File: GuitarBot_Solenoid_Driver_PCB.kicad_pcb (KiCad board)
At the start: 2 copper layers, 46 parts, among them J1 Screw_Terminal_01x02, J2 Screw_Terminal_01x16, J3 Screw_Terminal_01x16, J4 Screw_Terminal_01x04, Q1 NMOS, Q10 NMOS, Q11 NMOS, Q12 NMOS, Q13 NMOS, Q14 NMOS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

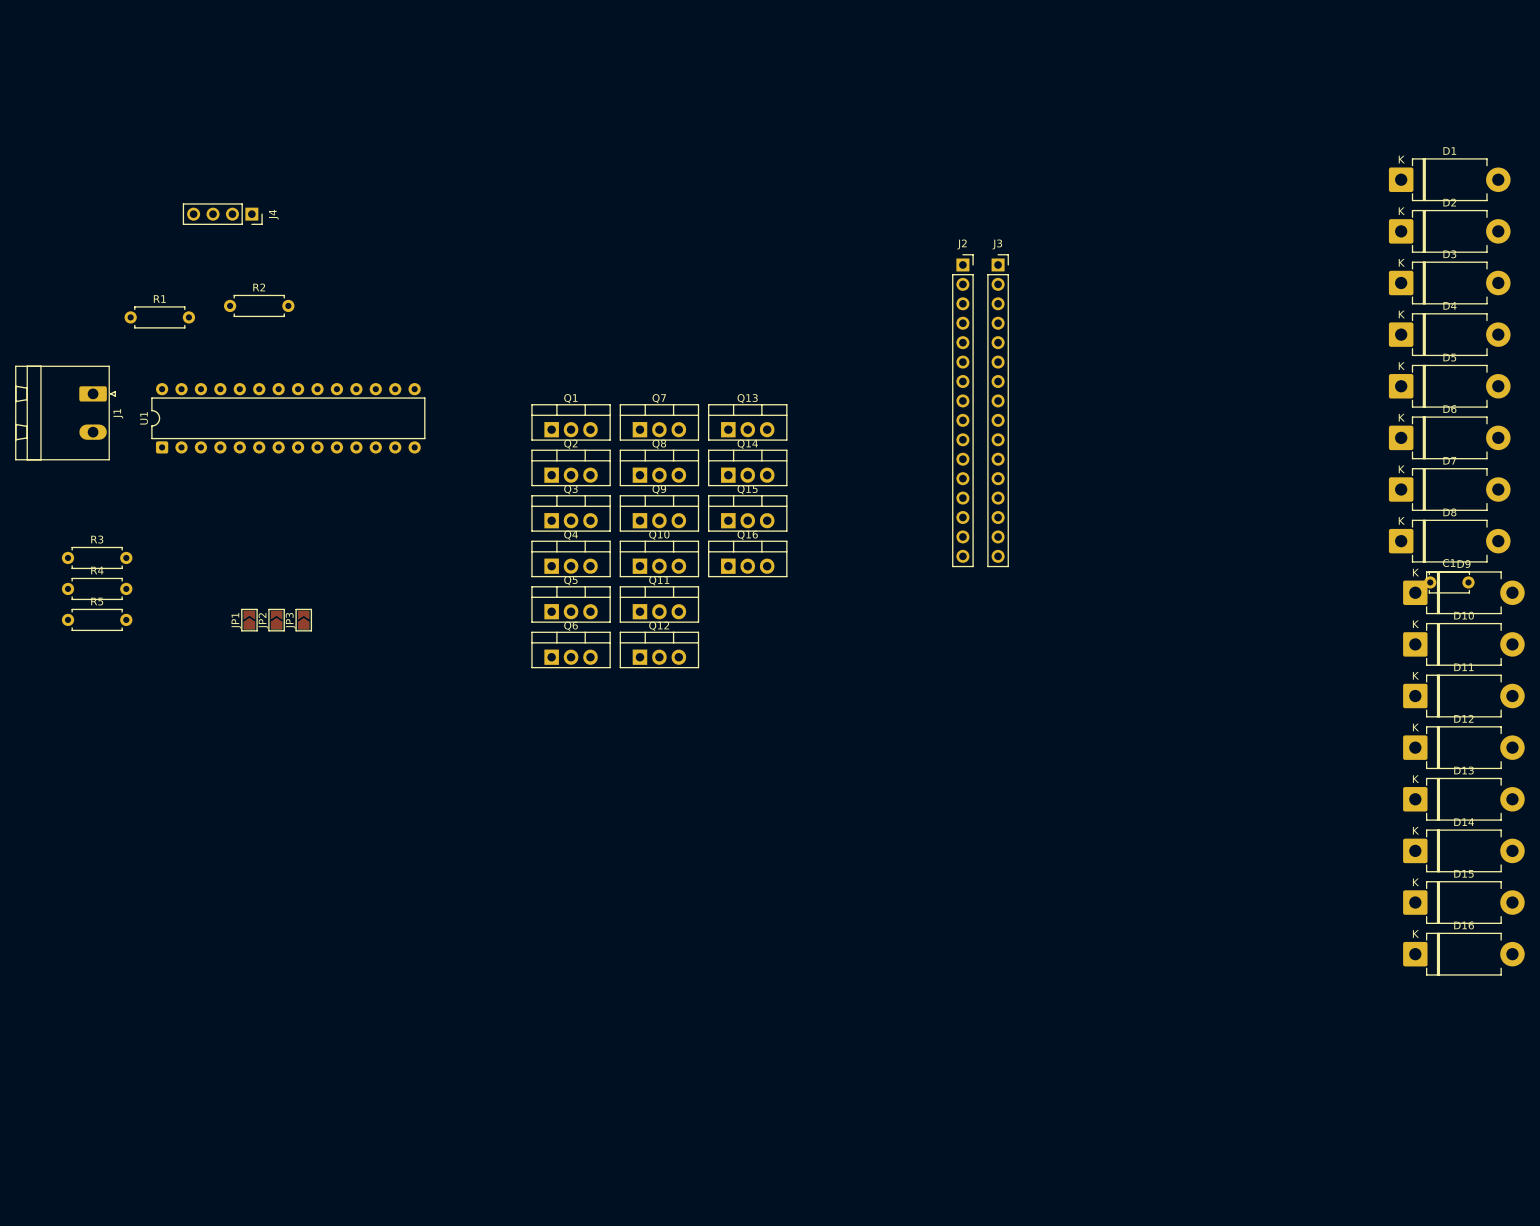
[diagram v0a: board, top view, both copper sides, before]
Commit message: Started pcb layout and updated schematic
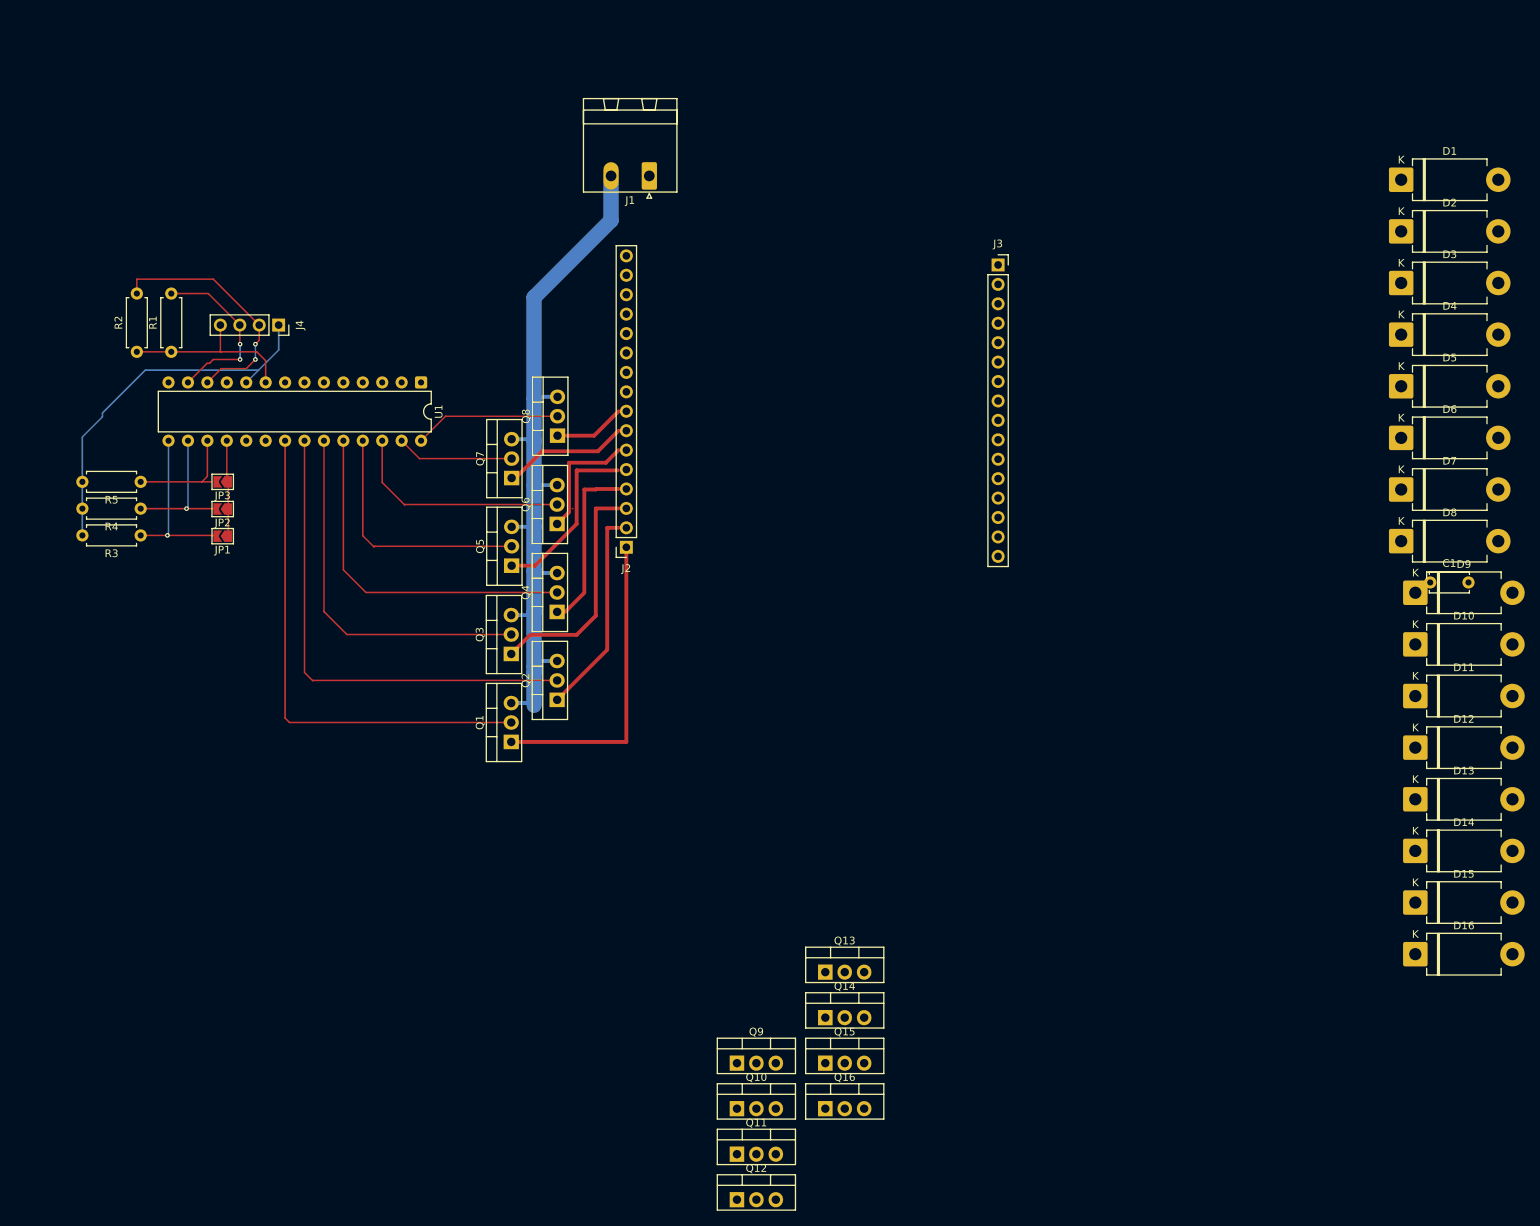
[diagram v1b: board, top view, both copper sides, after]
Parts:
- moved J1 78.1 mm to (122.0, 55.5), turned to 180 degrees
- moved Q14 72.0 mm to (145.0, 165.6)
- moved Q11 72.0 mm to (133.5, 183.4)
- moved Q12 72.0 mm to (133.5, 189.3)
- moved Q13 72.0 mm to (145.0, 159.6)
- moved Q15 72.0 mm to (145.0, 171.5)
- moved Q9 72.0 mm to (133.5, 171.5)
- moved Q10 72.0 mm to (133.5, 177.4)
- moved Q16 72.0 mm to (145.0, 177.4)
- moved J2 57.4 mm to (119.0, 104.0), turned to 180 degrees
- moved Q1 41.2 mm to (104.0, 129.5), turned to 90 degrees
- moved U1 34.9 mm to (92.2, 82.5), turned to -90 degrees
- moved Q2 29.4 mm to (110.0, 124.0), turned to 90 degrees
- moved JP3 21.0 mm to (66.2, 95.5), turned to 180 degrees
- moved R5 20.4 mm to (55.5, 95.5), turned to 180 degrees
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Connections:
- Q1 pad 1: Net-(D8-A) -> Net-(D1-A)
- Q2 pad 1: Net-(D7-A) -> Net-(D2-A)
- Q3 pad 1: Net-(D6-A) -> Net-(D3-A)
- Q4 pad 1: Net-(D5-A) -> Net-(D4-A)
- Q5 pad 1: Net-(D4-A) -> Net-(D5-A)
- Q6 pad 1: Net-(D3-A) -> Net-(D6-A)
- Q7 pad 1: Net-(D2-A) -> Net-(D7-A)
- Q8 pad 1: Net-(D1-A) -> Net-(D8-A)
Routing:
- net GNDPWR: track 0.00 -> 153.1 mm
- net /Sol1: track 0.00 -> 66.1 mm
- net /Sol2: track 0.00 -> 63.8 mm
- net /Sol3: track 0.00 -> 48.1 mm
- net /Sol4: track 0.00 -> 46.1 mm
- net Net-(D1-A): track 0.00 -> 40.5 mm
- net +3.3V: track 0.00 -> 37.0 mm
- net /SDK: track 0.00 -> 32.6 mm, vias 0 -> 2
- net /Sol5: track 0.00 -> 32.5 mm
- net Net-(D3-A): track 0.00 -> 30.2 mm
- net /Sol6: track 0.00 -> 29.6 mm
- net Net-(D2-A): track 0.00 -> 26.7 mm
- net Net-(D5-A): track 0.00 -> 23.3 mm
- net /SDA: track 0.00 -> 23.2 mm, vias 0 -> 2
- net Net-(D4-A): track 0.00 -> 22.6 mm
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
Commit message: Fixed NMOS symbol in schematic. Finished wiring the PCB
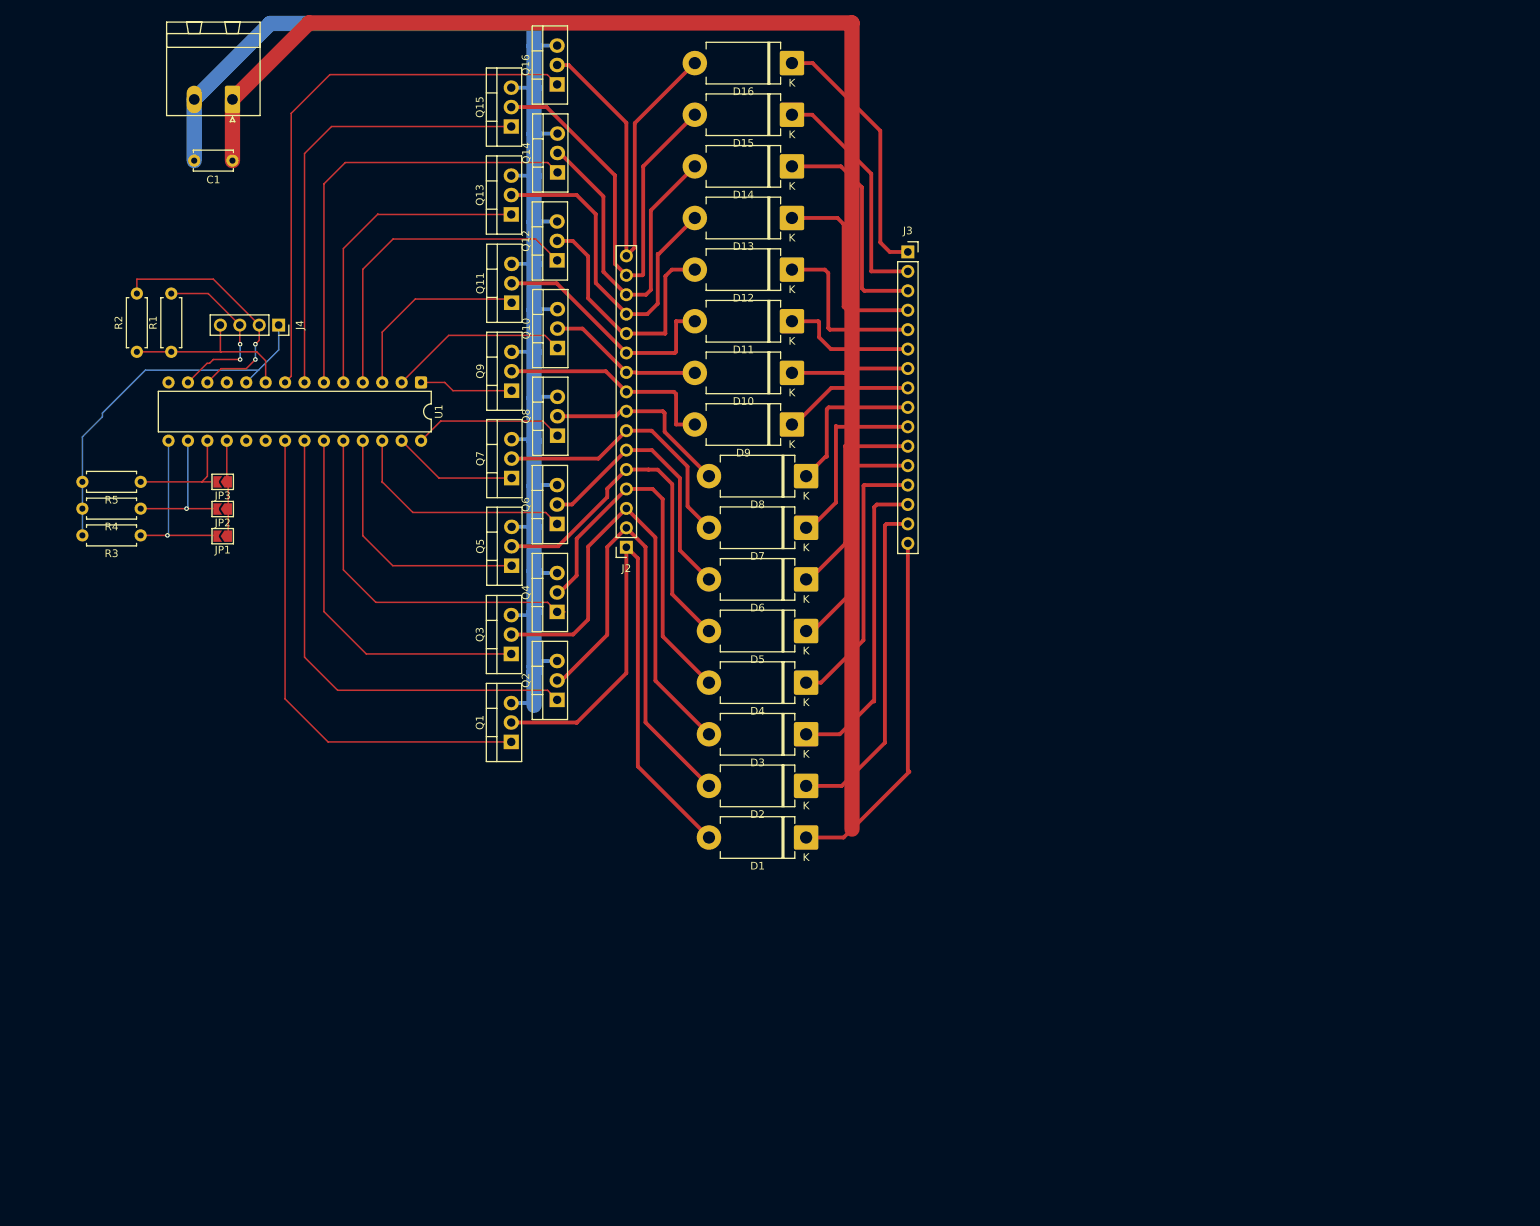
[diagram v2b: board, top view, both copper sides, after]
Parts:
- moved C1 166.0 mm to (67.5, 53.5), turned to 180 degrees
- moved D16 142.2 mm to (140.7, 40.8), turned to 180 degrees
- moved Q16 138.4 mm to (110.0, 43.5), turned to 90 degrees
- moved D15 131.3 mm to (140.7, 47.5), turned to 180 degrees
- moved Q15 129.2 mm to (104.0, 49.0), turned to 90 degrees
- moved Q12 125.0 mm to (110.0, 66.5), turned to 90 degrees
- moved D14 121.0 mm to (140.7, 54.2), turned to 180 degrees
- moved D1 116.0 mm to (142.5, 142.0), turned to 180 degrees
- moved Q14 115.9 mm to (110.0, 55.0), turned to 90 degrees
- moved Q11 115.2 mm to (104.0, 72.1), turned to 90 degrees
- moved D13 111.4 mm to (140.7, 61.0), turned to 180 degrees
- moved Q13 107.2 mm to (104.0, 60.5), turned to 90 degrees
- moved D2 106.3 mm to (142.5, 135.2), turned to 180 degrees
- moved D12 102.7 mm to (140.7, 67.8), turned to 180 degrees
- moved Q10 102.2 mm to (110.0, 78.0), turned to 90 degrees
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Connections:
- Q1 pad 1: Net-(D1-A) -> /Sol1
- Q1 pad 2: /Sol1 -> Net-(D1-A)
- Q10 pad 1: Net-(D10-A) -> /Sol10
- Q10 pad 2: /Sol10 -> Net-(D10-A)
- Q11 pad 1: Net-(D11-A) -> /Sol11
- Q11 pad 2: /Sol11 -> Net-(D11-A)
- Q12 pad 1: Net-(D12-A) -> /Sol12
- Q12 pad 2: /Sol12 -> Net-(D12-A)
- Q13 pad 1: Net-(D13-A) -> /Sol13
- Q13 pad 2: /Sol13 -> Net-(D13-A)
- Q14 pad 1: Net-(D14-A) -> /Sol14
- Q14 pad 2: /Sol14 -> Net-(D14-A)
- Q15 pad 1: Net-(D15-A) -> /Sol15
- Q15 pad 2: /Sol15 -> Net-(D15-A)
- Q16 pad 1: Net-(D16-A) -> /Sol16
- Q16 pad 2: /Sol16 -> Net-(D16-A)
- Q2 pad 1: Net-(D2-A) -> /Sol2
- Q2 pad 2: /Sol2 -> Net-(D2-A)
- Q3 pad 1: Net-(D3-A) -> /Sol3
- Q3 pad 2: /Sol3 -> Net-(D3-A)
- Q4 pad 1: Net-(D4-A) -> /Sol4
- Q4 pad 2: /Sol4 -> Net-(D4-A)
- Q5 pad 1: Net-(D5-A) -> /Sol5
- Q5 pad 2: /Sol5 -> Net-(D5-A)
- Q6 pad 1: Net-(D6-A) -> /Sol6
- Q6 pad 2: /Sol6 -> Net-(D6-A)
- Q7 pad 1: Net-(D7-A) -> /Sol7
- Q7 pad 2: /Sol7 -> Net-(D7-A)
- Q8 pad 1: Net-(D8-A) -> /Sol8
- Q8 pad 2: /Sol8 -> Net-(D8-A)
- Q9 pad 1: Net-(D9-A) -> /Sol9
- Q9 pad 2: /Sol9 -> Net-(D9-A)
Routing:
- net +12V: track 0.00 -> 665.5 mm
- net GNDPWR: track 153.1 -> 244.0 mm
- net /Sol16: track 0.00 -> 72.9 mm
- net /Sol15: track 0.00 -> 59.1 mm
- net Net-(D16-A): track 0.00 -> 58.5 mm
- net /Sol14: track 0.00 -> 58.2 mm
- net Net-(D15-A): track 0.00 -> 56.9 mm
- net Net-(D13-A): track 0.00 -> 44.8 mm
- net Net-(D14-A): track 0.00 -> 44.4 mm
- net /Sol12: track 0.00 -> 43.0 mm
- net /Sol13: track 0.00 -> 42.0 mm
- net Net-(D1-A): track 40.5 -> 76.7 mm
- net Net-(D2-A): track 26.7 -> 62.3 mm
- net Net-(D12-A): track 0.00 -> 34.1 mm
- net Net-(D11-A): track 0.00 -> 31.8 mm
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
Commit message: Finished feb15 updates to layout
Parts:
- removed J1: Screw_Terminal_01x02, Connector_Phoenix_MSTB:PhoenixContact_MSTBA_2,5_2-G_1x02_P5.00mm_Horizontal
- removed J2, J3: Screw_Terminal_01x16, Connector_PinSocket_2.54mm:PinSocket_1x16_P2.54mm_Vertical
- removed J4: Screw_Terminal_01x04, Connector_PinSocket_2.54mm:PinSocket_1x04_P2.54mm_Vertical
- added F1: Polyfuse, Fuse:Fuse_BelFuse_0ZRE0005FF_L8.3mm_W3.8mm, F.Cu at (165.5, 64.2)
- added J3V3: Screw_Terminal_01x02, TerminalBlock:TerminalBlock_Xinya_XY308-2.54-2P_1x02_P2.54mm_Horizontal, F.Cu at (70.5, 42.2)
- added JINT1: Screw_Terminal_01x02, TerminalBlock:TerminalBlock_Xinya_XY308-2.54-2P_1x02_P2.54mm_Horizontal, F.Cu at (70.0, 140.6)
- added JMUX1: Screw_Terminal_01x02, TerminalBlock:TerminalBlock_Xinya_XY308-2.54-2P_1x02_P2.54mm_Horizontal, F.Cu at (63.0, 42.2)
- added JSOL1: Screw_Terminal_01x16, TerminalBlock:TerminalBlock_Xinya_XY308-2.54-16P_1x16_P2.54mm_Horizontal, F.Cu at (125.0, 112.1)
- added JSOL2: Screw_Terminal_01x16, TerminalBlock:TerminalBlock_Xinya_XY308-2.54-16P_1x16_P2.54mm_Horizontal, F.Cu at (165.2, 112.0)
- added JSOL_PWR1: Screw_Terminal_01x02, TerminalBlock:TerminalBlock_MaiXu_MX126-5.0-02P_1x02_P5.00mm, F.Cu at (168.1, 42.5)
- added R10: 100k, Resistor_THT:R_Axial_DIN0207_L6.3mm_D2.5mm_P7.62mm_Horizontal, F.Cu at (93.0, 137.0)
- added R11: 100k, Resistor_THT:R_Axial_DIN0207_L6.3mm_D2.5mm_P7.62mm_Horizontal, F.Cu at (93.0, 131.0)
- added R12: 100k, Resistor_THT:R_Axial_DIN0207_L6.3mm_D2.5mm_P7.62mm_Horizontal, F.Cu at (93.0, 124.0)
- added R13: 100k, Resistor_THT:R_Axial_DIN0207_L6.3mm_D2.5mm_P7.62mm_Horizontal, F.Cu at (93.0, 118.0)
- added R14: 100k, Resistor_THT:R_Axial_DIN0207_L6.3mm_D2.5mm_P7.62mm_Horizontal, F.Cu at (93.0, 111.0)
- added R15: 100k, Resistor_THT:R_Axial_DIN0207_L6.3mm_D2.5mm_P7.62mm_Horizontal, F.Cu at (93.0, 105.0)
- added R16: 100k, Resistor_THT:R_Axial_DIN0207_L6.3mm_D2.5mm_P7.62mm_Horizontal, F.Cu at (93.2, 98.0)
- added R17: 100k, Resistor_THT:R_Axial_DIN0207_L6.3mm_D2.5mm_P7.62mm_Horizontal, F.Cu at (93.2, 90.0)
- added R18: 100k, Resistor_THT:R_Axial_DIN0207_L6.3mm_D2.5mm_P7.62mm_Horizontal, F.Cu at (93.2, 83.3)
- added R19: 100k, Resistor_THT:R_Axial_DIN0207_L6.3mm_D2.5mm_P7.62mm_Horizontal, F.Cu at (93.2, 76.7)
- added R20: 100k, Resistor_THT:R_Axial_DIN0207_L6.3mm_D2.5mm_P7.62mm_Horizontal, F.Cu at (93.2, 70.1)
- added R21: 100k, Resistor_THT:R_Axial_DIN0207_L6.3mm_D2.5mm_P7.62mm_Horizontal, F.Cu at (93.2, 63.5)
- added R22: 100k, Resistor_THT:R_Axial_DIN0207_L6.3mm_D2.5mm_P7.62mm_Horizontal, F.Cu at (93.2, 56.9)
- added R23: 100k, Resistor_THT:R_Axial_DIN0207_L6.3mm_D2.5mm_P7.62mm_Horizontal, F.Cu at (93.2, 50.3)
- added R24: 100k, Resistor_THT:R_Axial_DIN0207_L6.3mm_D2.5mm_P7.62mm_Horizontal, F.Cu at (93.2, 43.7)
- added R6: 10k, Resistor_THT:R_Axial_DIN0207_L6.3mm_D2.5mm_P7.62mm_Horizontal, F.Cu at (58.2, 124.6)
- added R7: 10k, Resistor_THT:R_Axial_DIN0207_L6.3mm_D2.5mm_P7.62mm_Horizontal, F.Cu at (65.8, 129.9)
- added R8: 10k, Resistor_THT:R_Axial_DIN0207_L6.3mm_D2.5mm_P7.62mm_Horizontal, F.Cu at (65.8, 135.1)
- added R9: 100k, Resistor_THT:R_Axial_DIN0207_L6.3mm_D2.5mm_P7.62mm_Horizontal, F.Cu at (93.2, 144.0)
- moved C1 99.8 mm to (167.3, 51.4)
- moved R5 24.0 mm to (58.2, 119.3), turned to 0 degrees
- moved R4 15.3 mm to (58.2, 114.0), turned to 0 degrees
- moved D10 15.0 mm to (155.3, 84.0)
- moved D11 15.0 mm to (155.3, 77.2)
- moved D12 15.0 mm to (155.3, 70.5)
- moved D13 15.0 mm to (155.3, 63.8)
- moved D14 15.0 mm to (155.3, 57.0)
- moved D15 15.0 mm to (155.3, 50.2)
- moved D16 15.0 mm to (155.3, 43.5)
- moved D9 15.0 mm to (155.3, 90.8)
- moved Q1 14.8 mm to (104.9, 144.3), turned to 0 degrees
- moved Q2 14.6 mm to (104.9, 137.7), turned to 0 degrees
- moved D8 13.3 mm to (155.3, 98.0)
- moved Q3 13.1 mm to (104.9, 131.1), turned to 0 degrees
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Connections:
- C1 pad 1: +12V -> Net-(JSOL_PWR1-Pin_1)
- U1 pad 18: +3.3V -> Net-(U1-~{RESET})
- U1 pad 19: +3.3V -> Net-(JINT1-Pin_1)
- U1 pad 20: +3.3V -> Net-(JINT1-Pin_2)
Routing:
- net +12V: track 665.5 -> 178.6 mm
- net GNDPWR: track 244.0 -> 378.6 mm
- net +3.3V: track 37.0 -> 104.5 mm
- net Net-(JINT1-Pin_2): track 0.00 -> 57.0 mm, vias 0 -> 1
- net Net-(JINT1-Pin_1): track 0.00 -> 54.6 mm, vias 0 -> 1
- net Net-(U1-~{RESET}): track 0.00 -> 30.2 mm, vias 0 -> 1
- net /SDA: track 23.2 -> 49.2 mm, vias 2 -> 0
- net Net-(D10-A): track 20.3 -> 39.8 mm
- net /SDK: track 32.6 -> 50.4 mm, vias 2 -> 0
- net Net-(JSOL_PWR1-Pin_1): track 0.00 -> 17.0 mm
- net Net-(D14-A): track 44.4 -> 61.1 mm
- net Net-(D1-A): track 76.7 -> 62.7 mm
- net Net-(D8-A): track 25.0 -> 38.7 mm
- net Net-(D12-A): track 34.1 -> 46.6 mm
- net Net-(JP3-B): track 14.9 -> 27.0 mm, vias 0 -> 1
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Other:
- board text added: "${REFERENCE}"
